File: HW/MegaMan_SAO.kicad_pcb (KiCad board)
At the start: 2 copper layers, 77.5 x 60 mm, 5 parts

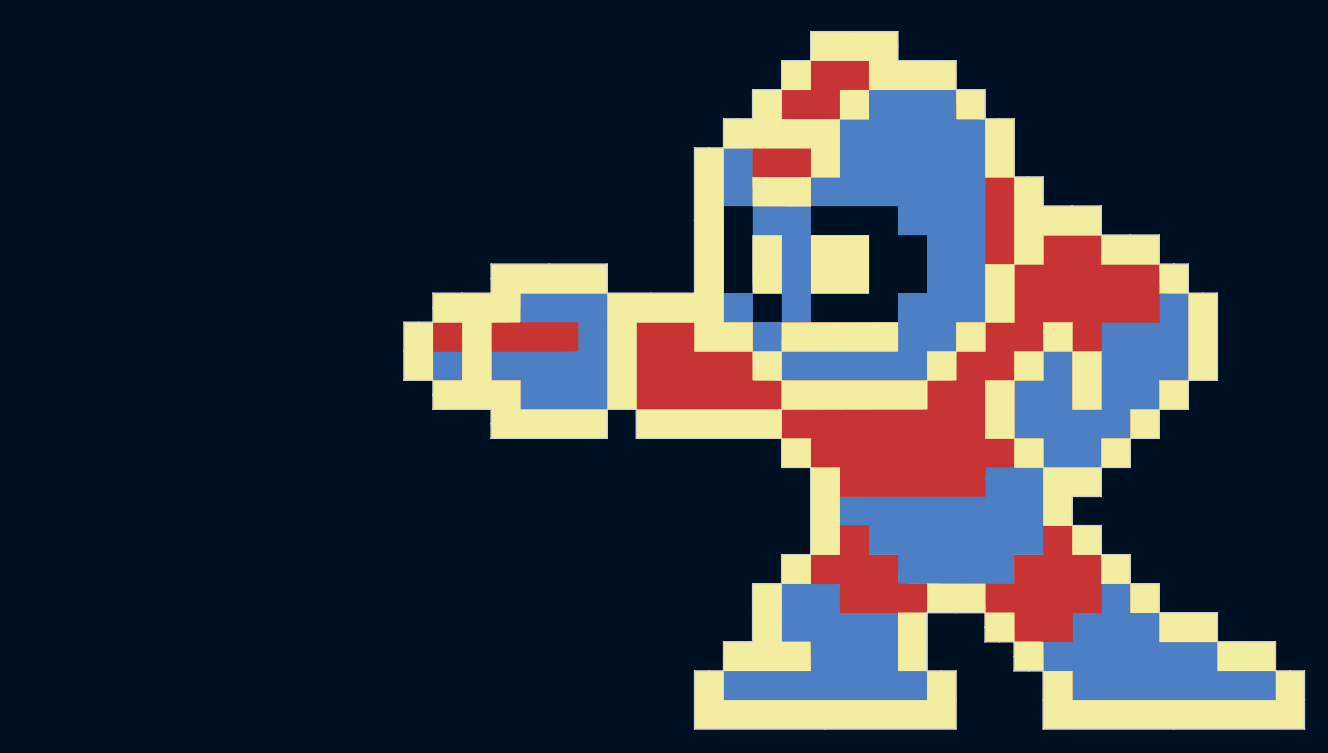
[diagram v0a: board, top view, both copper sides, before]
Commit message: Added footprints and library for LEDs and header
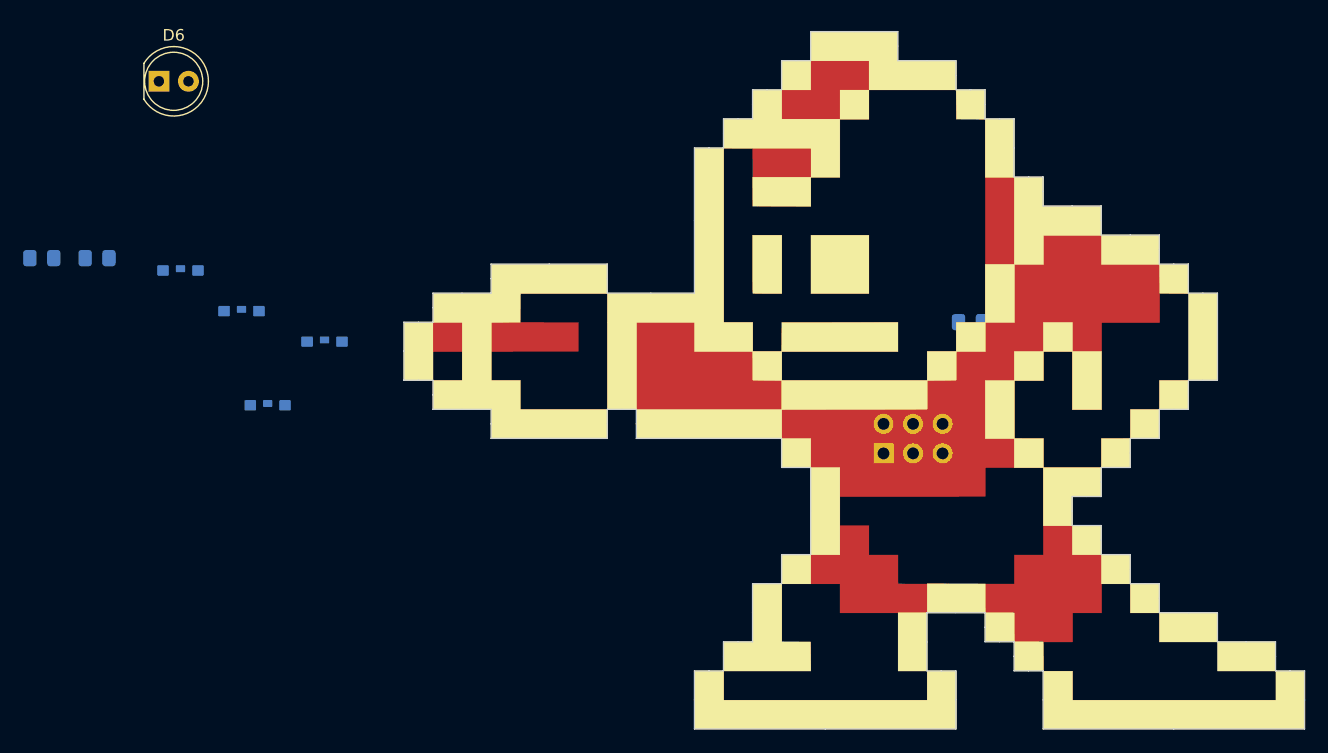
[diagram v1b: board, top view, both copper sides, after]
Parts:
- removed the G*** at (100.0, 100.0) (x5)
- added D1: WHT_LED, MegaMan_SAO:1204_SIDE_VIEW_LED, B.Cu at (100.0, 96.8)
- added D2: WHT_LED, MegaMan_SAO:1204_SIDE_VIEW_LED, B.Cu at (49.5, 102.2)
- added D3: WHT_LED, MegaMan_SAO:1204_SIDE_VIEW_LED, B.Cu at (42.0, 90.6)
- added D4: WHT_LED, MegaMan_SAO:1204_SIDE_VIEW_LED, B.Cu at (54.4, 96.7)
- added D5: WHT_LED, MegaMan_SAO:1204_SIDE_VIEW_LED, B.Cu at (47.3, 94.1)
- added D6: YLW_LED, LED_THT:LED_D5.0mm, F.Cu at (40.2, 74.3)
- added G***: B.Mask, MegaMan_SAO:B.Mask_g4150, F.Cu at (100.0, 100.0)
- added G***: F.Silk, MegaMan_SAO:F.Silk_g4158, F.Cu at (100.0, 100.0)
- added G***: F.Mask, MegaMan_SAO:F.Mask_g4156, F.Cu at (100.0, 100.0)
- added G***: F.Cu, MegaMan_SAO:F.Cu_g4154, F.Cu at (100.0, 100.0)
- added R1: 50R, Resistor_SMD:R_0805_2012Metric_Pad1.15x1.40mm_HandSolder, B.Cu at (110.0, 95.0)
- added R2: 50R, Resistor_SMD:R_0805_2012Metric_Pad1.15x1.40mm_HandSolder, B.Cu at (30.1, 89.5)
- added R3: 50R, Resistor_SMD:R_0805_2012Metric_Pad1.15x1.40mm_HandSolder, B.Cu at (34.9, 89.5)
- added X1: Badgelife_sao_connector_v169bis, MegaMan_SAO:Badgelife-SAOv169-SAO-2x3, F.Cu at (105.0, 105.0)

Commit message: placing parts
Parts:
- D6: footprint LED_THT:LED_D5.0mm -> LED_THT:LED_D5.0mm_Horizontal_O6.35mm_Z3.0mm
- moved R2 63.9 mm to (93.0, 101.0), turned to 90 degrees
- moved D2 59.7 mm to (108.0, 90.0), turned to 270 degrees
- moved D3 58.4 mm to (100.0, 83.2)
- moved D5 41.5 mm to (88.8, 95.0), turned to 135 degrees
- moved R3 40.5 mm to (74.8, 96.2)
- moved D4 39.4 mm to (93.0, 88.8), turned to 270 degrees
- moved D6 36.7 mm to (67.5, 98.8), turned to 90 degrees
- moved R1 3.47 mm to (107.0, 96.8)

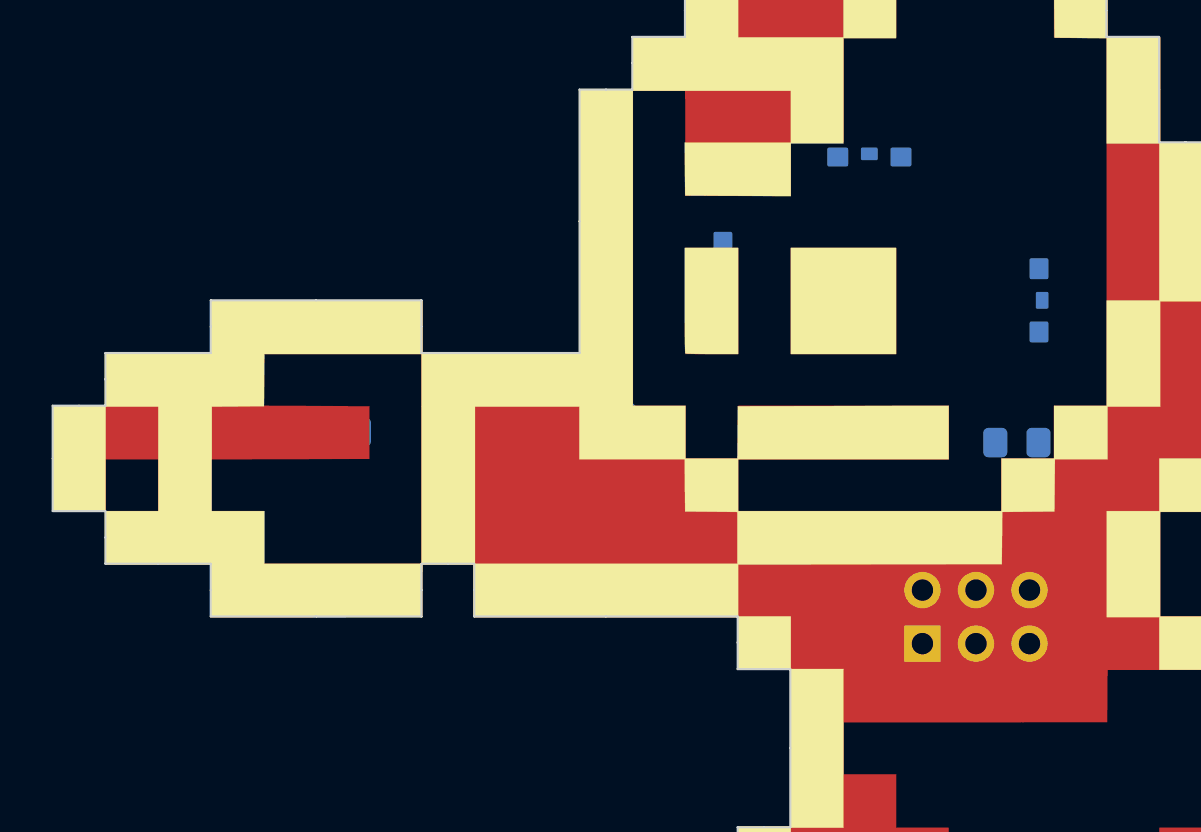
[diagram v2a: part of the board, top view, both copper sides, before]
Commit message: Added B.cu Keep out, B.Cu ground pour
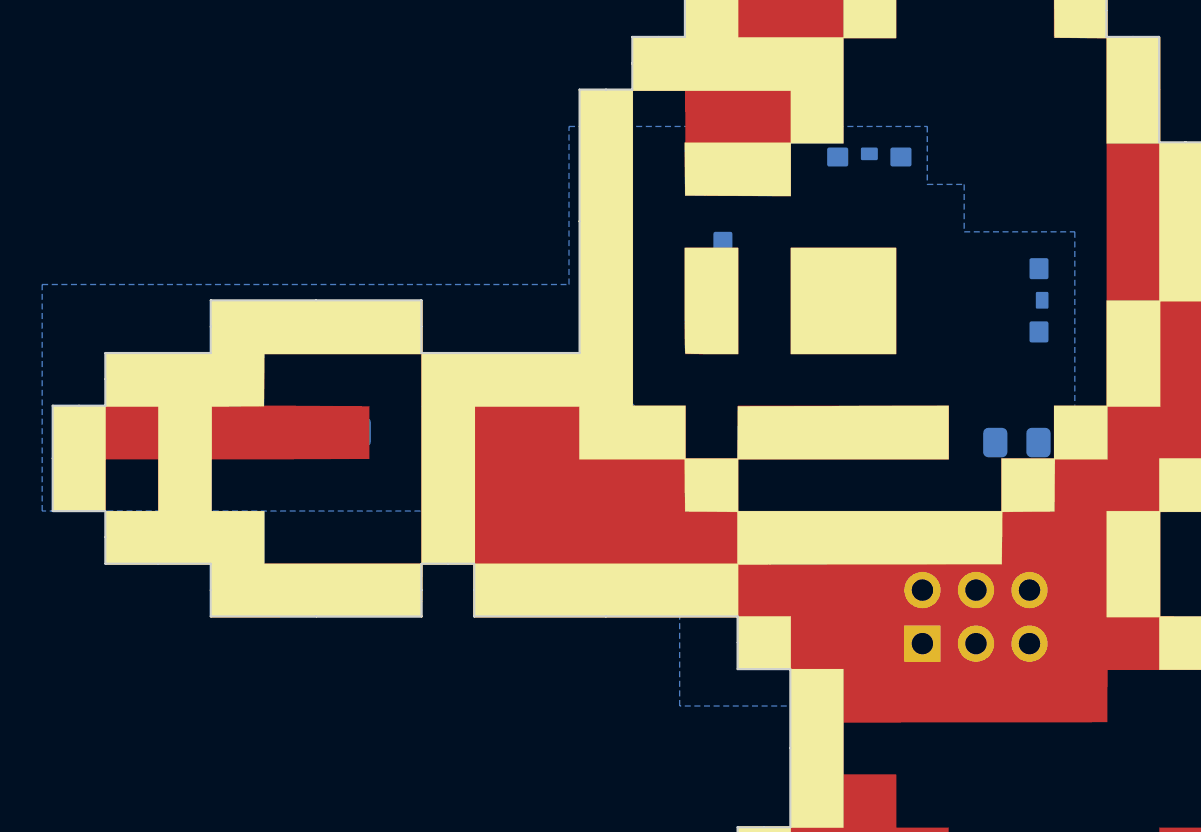
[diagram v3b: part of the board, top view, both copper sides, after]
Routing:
- added copper zone on B.Cu, net GND
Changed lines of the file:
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@@
     (last_trace_width 0.25)
     (trace_clearance 0.2)
-    (zone_clearance 0.508)
+    (zone_clearance 0.0254)
     (zone_45_only no)
     (trace_min 0.2)
@@
   (gr_line (start 86.25 130) (end 86.25 127.5) (layer Edge.Cuts) (width 0.1))
   (gr_line (start 86.25 127.5) (end 86.25 127.5) (layer Edge.Cuts) (width 0.1))
+  (zone (net 0) (net_name "") (layer B.Cu) (hatch full 0.508)
+    (connect_pads (clearance 0.508))
+    (min_thickness 0.254)
+    (keepout (tracks not_allowed) (vias not_allowed) (copperpour not_allowed))
+    (fill (arc_segments 32) (thermal_gap 0.508) (thermal_bridge_width 0.508))
+    (polygon
+      (pts
+        (xy 103.78 85) (xy 96.26 85) (xy 96.26 87.56) (xy 101.26 87.57) (xy 101.26 92.5)
+        (xy 96.26 92.5) (xy 96.26 95.06) (xy 103.78 95.06) (xy 103.78 92.56) (xy 106.27 92.56)
+        (xy 106.27 87.5) (xy 103.78 87.5)
+      )
+    )
+  )
+  (zone (net 0) (net_name "") (layer B.Cu) (hatch full 0.508)
+    (connect_pads (clearance 0.508))
+    (min_thickness 0.254)
+    (keepout (tracks not_allowed) (vias not_allowed) (copperpour not_allowed))
+    (fill (arc_segments 32) (thermal_gap 0.508) (thermal_bridge_width 0.508))
+    (polygon
+      (pts
+        (xy 91.29 85) (xy 88.73 85) (xy 88.76 92.56) (xy 91.23 92.56) (xy 91.22 95.05)
+        (xy 93.79 95.05) (xy 93.79 92.5) (xy 91.29 92.5)
+      )
+    )
+  )
+  (zone (net 1) (net_name GND) (layer B.Cu) (hatch edge 0.508)
+    (connect_pads (clearance 0.0254))
+    (min_thickness 0.0254)
+    (fill yes (arc_segments 32) (thermal_gap 0.508) (thermal_bridge_width 0.508))
+    (polygon
+      (pts
+        (xy 102.75 84.5) (xy 104.5 84.5) (xy 104.5 86.75) (xy 109.75 86.75) (xy 109.75 109.25)
+        (xy 91 109.25) (xy 91 100) (xy 60.75 100) (xy 60.75 89.25) (xy 85.75 89.25)
+        (xy 85.75 81.75) (xy 102.75 81.75)
+      )
+    )
+  )
 )

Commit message: added traces, fixed up ground pour
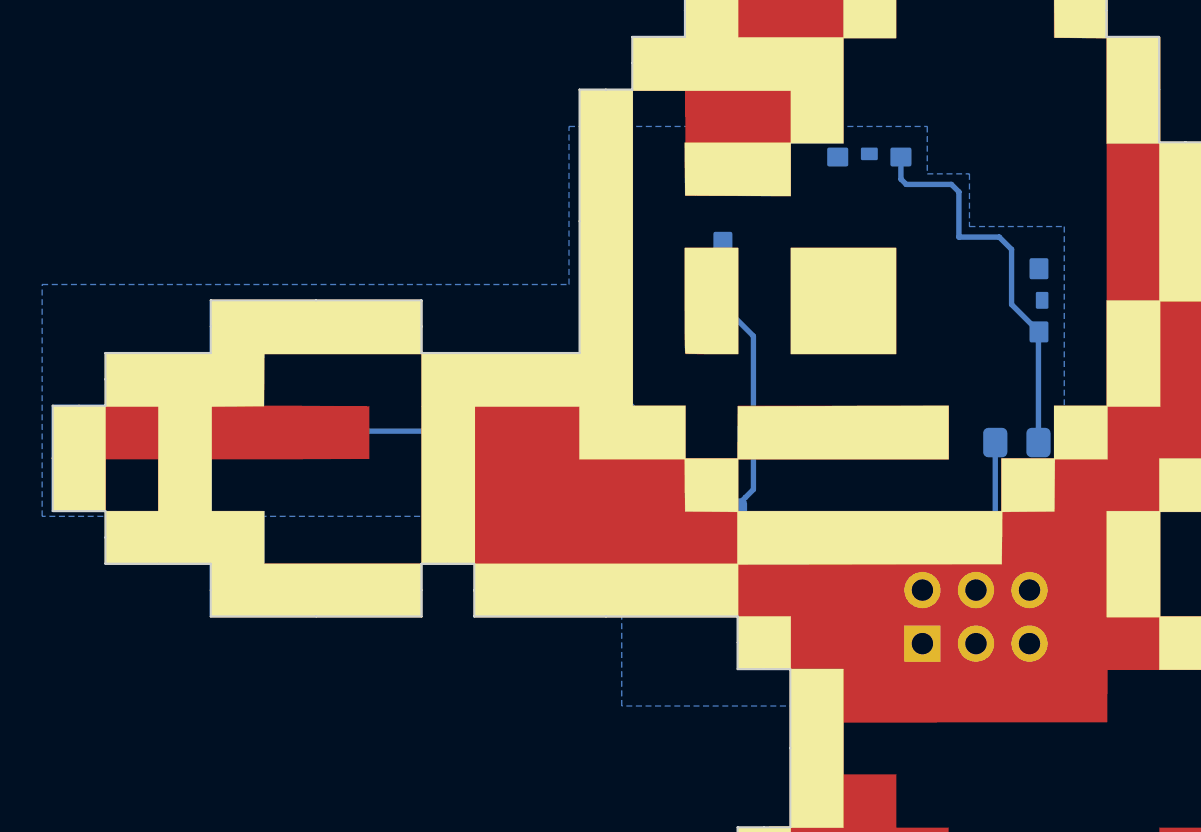
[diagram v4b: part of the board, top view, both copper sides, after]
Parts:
- moved R3 15.5 mm to (89.5, 101.0), turned to 90 degrees
- moved R2 0.50 mm to (93.5, 101.0)
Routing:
- net Net-(D6-Pad2): track 0.00 -> 24.0 mm
- net VCC: track 0.00 -> 22.2 mm
- net Net-(D4-Pad2): track 0.00 -> 20.3 mm
- net Net-(D1-Pad2): track 0.00 -> 18.7 mm
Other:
- net class Default: clearance 0.2 -> 0.1524; trace_width 0.25 -> 0.1524
- rule trace_clearance: 0.2 -> 0.1524
- rule trace_min: 0.2 -> 0.1524

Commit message: Netlist, B.Silk Art, lib files
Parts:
- added G***: LOGO, MegaMan_SAO:B.Cu_g4148, F.Cu at (100.0, 100.0)
- added G***: LOGO, MegaMan_SAO:B.Silk_g4152, F.Cu at (100.0, 100.0)
- added G***: LOGO, MegaMan_SAO:B.Silk_g4152, F.Cu at (149.9, 89.0)
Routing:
- net Net-(D1-Pad2): track 18.7 -> 30.7 mm
- added copper zone on F.Cu, net GND

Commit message: lots of art work changes
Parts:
- removed the G*** at (100.0, 100.0)
- G***: footprint MegaMan_SAO:B.Mask_g4150 -> MegaMan_SAO:B.Mask
- G***: footprint MegaMan_SAO:B.Silk_g4152 -> MegaMan_SAO:B.Silk
- moved G*** 51.1 mm to (100.0, 100.0)
- moved R3 3.85 mm to (93.0, 102.6), turned to 270 degrees
- moved R2 3.04 mm to (93.0, 98.0)
- renumbered G*** to B.Cu
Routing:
- net Net-(D6-Pad2): track 24.0 -> 28.6 mm
- net Net-(D4-Pad2): track 20.3 -> 19.8 mm
